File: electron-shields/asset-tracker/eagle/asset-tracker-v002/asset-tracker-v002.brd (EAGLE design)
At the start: 95.2 x 38.1 mm, 23 parts, among them J1 1X2-3.5MM, T1 DMG3415, U1 FGPMMOPA6H, U3 LIS3DHTR, X1 ELECTRON, X2 uFL

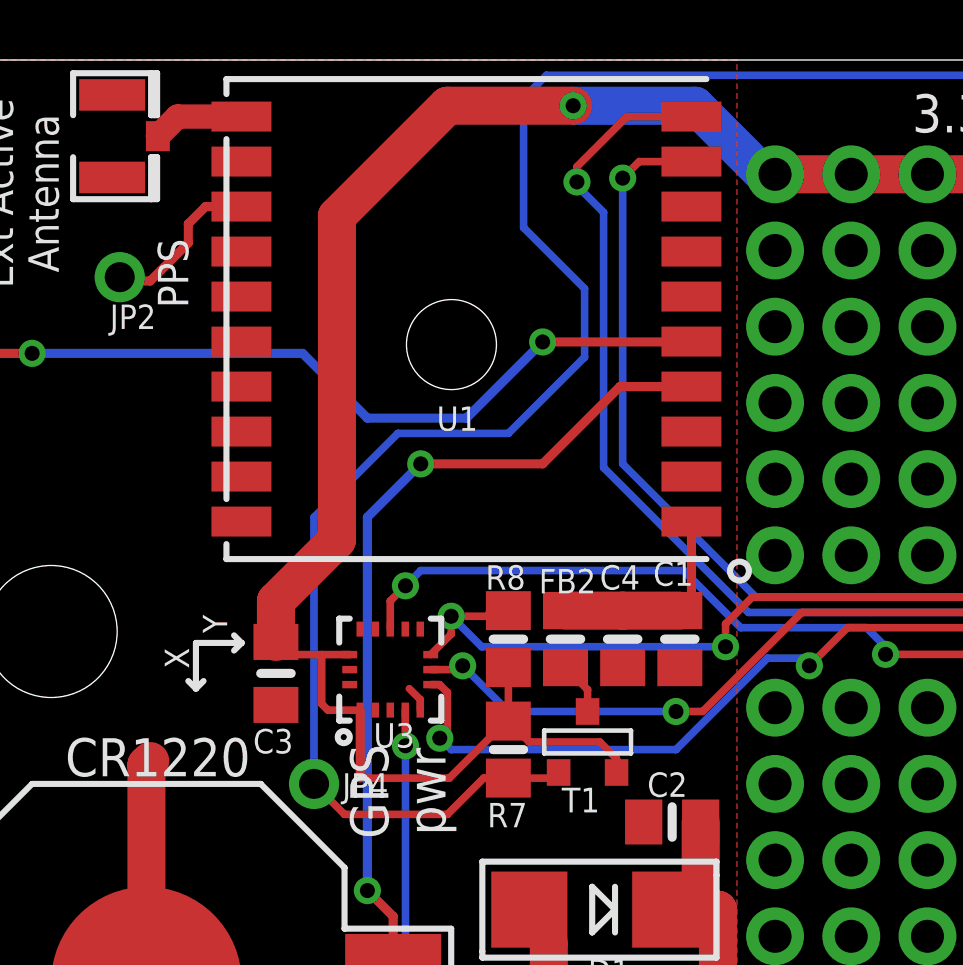
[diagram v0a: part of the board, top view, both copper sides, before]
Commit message: 3v3 trace widened
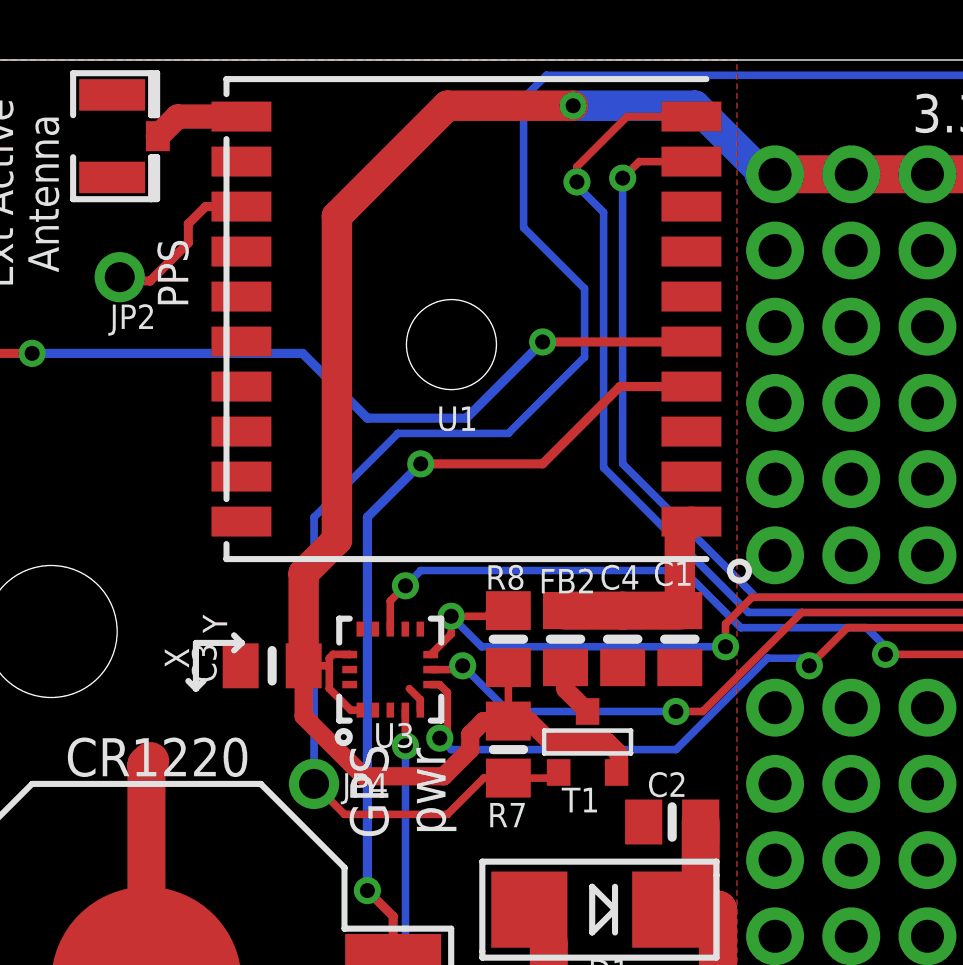
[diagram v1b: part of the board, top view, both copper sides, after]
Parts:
- moved C3 0.28 mm to (15.0, 17.9), turned to 180 degrees
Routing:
- net 3.3V: track 80.1 -> 81.5 mm
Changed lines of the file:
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@@
 <layer number="39" name="tKeepout" color="4" fill="11" visible="no" active="yes"/>
 <layer number="40" name="bKeepout" color="1" fill="11" visible="no" active="yes"/>
-<layer number="41" name="tRestrict" color="4" fill="10" visible="yes" active="yes"/>
+<layer number="41" name="tRestrict" color="4" fill="10" visible="no" active="yes"/>
 <layer number="42" name="bRestrict" color="1" fill="10" visible="no" active="yes"/>
 <layer number="43" name="vRestrict" color="2" fill="10" visible="no" active="yes"/>
@@
 <attribute name="VALUE" x="16.207" y="16.396" size="0.8128" layer="27" ratio="12"/>
 </element>
-<element name="C3" library="microbuilder" package="0805_10MGAP" value="0.1uF" x="15.113" y="17.653" smashed="yes" rot="R270">
-<attribute name="NAME" x="14.351" y="14.986" size="0.8128" layer="25" ratio="18"/>
-<attribute name="VALUE" x="14.859" y="19.177" size="0.8128" layer="27" ratio="10" rot="R270"/>
+<element name="C3" library="microbuilder" package="0805_10MGAP" value="0.1uF" x="14.986" y="17.907" smashed="yes" rot="R180">
+<attribute name="NAME" x="12.319" y="18.669" size="0.8128" layer="25" ratio="18" rot="R270"/>
+<attribute name="VALUE" x="16.51" y="18.161" size="0.8128" layer="27" ratio="10" rot="R180"/>
 </element>
 <element name="R8" library="microbuilder" package="0805-NO" value="10K" x="22.86" y="18.796" smashed="yes" rot="R270">
@@
 <wire x1="46.99" y1="27.051" x2="46.99" y2="24.13" width="1.27" layer="1"/>
 <wire x1="46.99" y1="24.13" x2="46.99" y2="21.59" width="1.27" layer="1"/>
-<wire x1="17.573" y1="18.28" x2="16.637" y2="18.28" width="0.254" layer="1"/>
-<wire x1="16.637" y1="18.28" x2="15.536" y2="18.28" width="0.254" layer="1"/>
-<wire x1="15.536" y1="18.28" x2="15.113" y2="18.703" width="0.254" layer="1"/>
-<wire x1="17.923" y1="16.43" x2="16.844" y2="16.43" width="0.254" layer="1"/>
-<wire x1="16.844" y1="16.43" x2="16.637" y2="16.637" width="0.254" layer="1"/>
-<wire x1="16.637" y1="16.637" x2="16.637" y2="18.28" width="0.254" layer="1"/>
-<wire x1="17.923" y1="16.43" x2="17.923" y2="14.163" width="0.3048" layer="1"/>
 <wire x1="46.99" y1="31.369" x2="46.99" y2="34.29" width="1.27" layer="1"/>
 <wire x1="46.99" y1="34.29" x2="44.45" y2="34.29" width="1.27" layer="1"/>
-<wire x1="15.113" y1="18.703" x2="15.113" y2="20.066" width="1.27" layer="1"/>
-<wire x1="15.113" y1="20.066" x2="17.145" y2="22.098" width="1.27" layer="1"/>
-<wire x1="17.145" y1="22.098" x2="17.145" y2="32.893" width="1.27" layer="1"/>
+<wire x1="17.145" y1="22.098" x2="17.145" y2="32.893" width="1.016" layer="1"/>
 <wire x1="22.86" y1="17.846" x2="22.86" y2="16.063" width="0.254" layer="1"/>
-<wire x1="22.86" y1="16.063" x2="23.556" y2="15.367" width="0.254" layer="1"/>
-<wire x1="23.556" y1="15.367" x2="25.908" y2="15.367" width="0.254" layer="1"/>
-<wire x1="25.908" y1="15.367" x2="26.4668" y2="14.8082" width="0.254" layer="1"/>
-<wire x1="26.4668" y1="14.8082" x2="26.4668" y2="14.351" width="0.254" layer="1"/>
 <wire x1="22.86" y1="16.063" x2="22.794" y2="16.063" width="0.254" layer="1"/>
-<wire x1="22.794" y1="16.063" x2="20.894" y2="14.163" width="0.254" layer="1"/>
-<wire x1="20.894" y1="14.163" x2="17.923" y2="14.163" width="0.254" layer="1"/>
-<wire x1="17.145" y1="32.893" x2="20.828" y2="36.576" width="1.27" layer="1"/>
-<wire x1="20.828" y1="36.576" x2="25.019" y2="36.576" width="1.27" layer="1"/>
+<wire x1="17.145" y1="32.893" x2="20.828" y2="36.576" width="1.016" layer="1"/>
+<wire x1="20.828" y1="36.576" x2="25.019" y2="36.576" width="1.016" layer="1"/>
 <via x="25.019" y="36.576" extent="1-16" drill="0.5"/>
-<wire x1="25.019" y1="36.576" x2="29.083" y2="36.576" width="1.27" layer="16"/>
-<wire x1="31.369" y1="34.29" x2="29.083" y2="36.576" width="1.27" layer="16"/>
+<wire x1="25.019" y1="36.576" x2="29.083" y2="36.576" width="1.016" layer="16"/>
+<wire x1="31.369" y1="34.29" x2="29.083" y2="36.576" width="1.016" layer="16"/>
 <wire x1="31.75" y1="34.29" x2="31.369" y2="34.29" width="1.27" layer="16"/>
+<wire x1="17.145" y1="22.098" x2="16.036" y2="20.989" width="1.016" layer="1"/>
+<wire x1="16.036" y1="20.989" x2="16.036" y2="18.034" width="1.016" layer="1"/>
+<wire x1="22.86" y1="16.063" x2="23.561" y2="16.063" width="0.6096" layer="1"/>
+<wire x1="23.561" y1="16.063" x2="24.257" y2="15.367" width="0.6096" layer="1"/>
+<wire x1="24.257" y1="15.367" x2="26.162" y2="15.367" width="0.6096" layer="1"/>
+<wire x1="26.162" y1="15.367" x2="26.543" y2="14.986" width="0.6096" layer="1"/>
+<wire x1="26.543" y1="14.986" x2="26.543" y2="14.4272" width="0.6096" layer="1"/>
+<wire x1="26.543" y1="14.4272" x2="26.4668" y2="14.351" width="0.6096" layer="1"/>
+<wire x1="18.034" y1="14.224" x2="20.701" y2="14.224" width="0.6096" layer="1"/>
+<wire x1="20.701" y1="14.224" x2="21.59" y2="15.113" width="0.6096" layer="1"/>
+<wire x1="21.59" y1="15.113" x2="21.59" y2="15.621" width="0.6096" layer="1"/>
+<wire x1="21.59" y1="15.621" x2="22.032" y2="16.063" width="0.6096" layer="1"/>
+<wire x1="22.032" y1="16.063" x2="22.86" y2="16.063" width="0.6096" layer="1"/>
+<wire x1="18.034" y1="14.224" x2="16.036" y2="16.222" width="0.6096" layer="1"/>
+<wire x1="16.036" y1="16.222" x2="16.036" y2="17.907" width="0.6096" layer="1"/>
+<wire x1="17.923" y1="16.43" x2="17.606" y2="16.43" width="0.254" layer="1"/>
+<wire x1="17.606" y1="16.43" x2="16.891" y2="17.145" width="0.254" layer="1"/>
+<wire x1="16.891" y1="17.145" x2="16.891" y2="17.907" width="0.254" layer="1"/>
+<wire x1="16.891" y1="17.907" x2="16.891" y2="18.161" width="0.254" layer="1"/>
+<wire x1="16.891" y1="18.161" x2="17.018" y2="18.288" width="0.254" layer="1"/>
+<wire x1="17.018" y1="18.288" x2="17.565" y2="18.288" width="0.254" layer="1"/>
+<wire x1="17.565" y1="18.288" x2="17.573" y2="18.28" width="0.254" layer="1"/>
+<wire x1="16.036" y1="18.034" x2="16.163" y2="17.907" width="0.254" layer="1"/>
+<wire x1="16.163" y1="17.907" x2="16.891" y2="17.907" width="0.254" layer="1"/>
+<wire x1="16.036" y1="18.034" x2="16.036" y2="17.907" width="0.254" layer="1"/>
 </signal>
 <signal name="VBACKUP">
@@
 <contactref element="FB2" pad="1"/>
 <contactref element="C4" pad="1"/>
-<wire x1="28.575" y1="19.746" x2="28.963" y2="20.134" width="0.3048" layer="1"/>
-<wire x1="28.963" y1="22.714" x2="28.963" y2="20.134" width="0.3048" layer="1"/>
 <wire x1="28.575" y1="19.746" x2="26.67" y2="19.746" width="1.27" layer="1"/>
 <wire x1="26.67" y1="19.746" x2="24.765" y2="19.746" width="1.27" layer="1"/>
+<wire x1="28.575" y1="19.746" x2="28.575" y2="22.326" width="1.016" layer="1"/>
+<wire x1="28.575" y1="22.326" x2="28.963" y2="22.714" width="1.016" layer="1"/>
 </signal>
 <signal name="ACCEL_CS">
@@
 <contactref element="T1" pad="1"/>
 <contactref element="FB2" pad="2"/>
-<wire x1="24.765" y1="17.846" x2="25.5016" y2="17.1094" width="0.254" layer="1"/>
-<wire x1="25.5016" y1="17.1094" x2="25.5016" y2="16.383" width="0.254" layer="1"/>
+<wire x1="25.5016" y1="16.383" x2="24.765" y2="17.1196" width="0.6096" layer="1"/>
+<wire x1="24.765" y1="17.1196" x2="24.765" y2="17.846" width="0.6096" layer="1"/>
 </signal>
 <signal name="N$10">
